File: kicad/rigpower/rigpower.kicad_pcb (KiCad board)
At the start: 2 copper layers, 66 x 54.6 mm, 11 parts, among them J1 Conn_01x02, J2 Conn_01x02, J3 Conn_01x02, J4 Conn_01x02, J5 Conn_01x02

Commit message: drawing improved
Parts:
- added REF**: SolderWirePad_single_0-8mmDrill, Wire_Pads:SolderWirePad_single_0-8mmDrill, B.Cu at (157.5, 111.1)
- added REF**: SolderWirePad_single_0-8mmDrill, Wire_Pads:SolderWirePad_single_0-8mmDrill, B.Cu at (163.2, 130.8)
- added REF**: SolderWirePad_single_0-8mmDrill, Wire_Pads:SolderWirePad_single_0-8mmDrill, B.Cu at (152.4, 130.8)
- added REF**: SolderWirePad_single_0-8mmDrill, Wire_Pads:SolderWirePad_single_0-8mmDrill, B.Cu at (144.1, 111.1)
- added REF**: SolderWirePad_single_0-8mmDrill, Wire_Pads:SolderWirePad_single_0-8mmDrill, B.Cu at (174.6, 111.1)
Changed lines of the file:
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@@
-(kicad_pcb (version 20171130) (host pcbnew 5.0.1)
+(kicad_pcb (version 20171130) (host pcbnew 5.1.0)
   (general
     (thickness 1.6)
-    (drawings 40)
+    (drawings 49)
     (tracks 10)
     (zones 0)
-    (modules 11)
+    (modules 16)
     (nets 11)
   )
@@
     (zone_45_only no)
     (trace_min 0.2)
-    (segment_width 0.2)
-    (edge_width 0.15)
     (via_size 0.8)
     (via_drill 0.4)
@@
     (uvia_min_size 0.2)
     (uvia_min_drill 0.1)
+    (edge_width 0.15)
+    (segment_width 0.2)
     (pcb_text_width 0.3)
     (pcb_text_size 1.5 1.5)
@@
     (mod_text_size 1 1)
     (mod_text_width 0.15)
-    (pad_size 1.7 1.7)
-    (pad_drill 1)
+    (pad_size 1.99898 1.99898)
+    (pad_drill 0)
     (pad_to_mask_clearance 0.051)
     (solder_mask_min_width 0.25)
@@
     (add_net "Net-(J5-Pad2)")
   )
+  (module Wire_Pads:SolderWirePad_single_0-8mmDrill (layer B.Cu)
+    (at 157.48 111.125)
+    (fp_text reference REF** (at 0 2.54) (layer B.SilkS) hide
+      (effects (font (size 1 1) (thickness 0.15)) (justify mirror))
+    )
+    (fp_text value SolderWirePad_single_0-8mmDrill (at 0 -2.54) (layer B.Fab)
+      (effects (font (size 1 1) (thickness 0.15)) (justify mirror))
+    )
+    (pad 1 smd circle (at 0 0) (size 1.99898 1.99898) (layers B.Cu B.Paste B.Mask))
+  )
+  (module Wire_Pads:SolderWirePad_single_0-8mmDrill (layer B.Cu)
+    (at 163.195 130.81)
+    (fp_text reference REF** (at 0 2.54) (layer B.SilkS) hide
+      (effects (font (size 1 1) (thickness 0.15)) (justify mirror))
+    )
+    (fp_text value SolderWirePad_single_0-8mmDrill (at 0 -2.54) (layer B.Fab)
+      (effects (font (size 1 1) (thickness 0.15)) (justify mirror))
+    )
+    (pad 1 smd circle (at 0 0) (size 1.99898 1.99898) (layers B.Cu B.Paste B.Mask))
+  )
+  (module Wire_Pads:SolderWirePad_single_0-8mmDrill (layer B.Cu)
+    (at 152.4 130.81)
+    (fp_text reference REF** (at 0 2.54) (layer B.SilkS) hide
+      (effects (font (size 1 1) (thickness 0.15)) (justify mirror))
+    )
+    (fp_text value SolderWirePad_single_0-8mmDrill (at 0 -2.54) (layer B.Fab)
+      (effects (font (size 1 1) (thickness 0.15)) (justify mirror))
+    )
+    (pad 1 smd circle (at 0 0) (size 1.99898 1.99898) (layers B.Cu B.Paste B.Mask))
+  )
+  (module Wire_Pads:SolderWirePad_single_0-8mmDrill (layer B.Cu)
+    (at 144.145 111.125)
+    (fp_text reference REF** (at 0 2.54) (layer B.SilkS) hide
+      (effects (font (size 1 1) (thickness 0.15)) (justify mirror))
+    )
+    (fp_text value SolderWirePad_single_0-8mmDrill (at 0 -2.54) (layer B.Fab)
+      (effects (font (size 1 1) (thickness 0.15)) (justify mirror))
+    )
+    (pad 1 smd circle (at 0 0) (size 1.99898 1.99898) (layers B.Cu B.Paste B.Mask))
+  )
+  (module Wire_Pads:SolderWirePad_single_0-8mmDrill (layer B.Cu)
+    (at 174.625 111.125)
+    (fp_text reference REF** (at 0 2.54) (layer B.SilkS) hide
+      (effects (font (size 1 1) (thickness 0.15)) (justify mirror))
+    )
+    (fp_text value SolderWirePad_single_0-8mmDrill (at 0 -2.54) (layer B.Fab)
+      (effects (font (size 1 1) (thickness 0.15)) (justify mirror))
+    )
+    (pad 1 smd circle (at 0 0) (size 1.99898 1.99898) (layers B.Cu B.Paste B.Mask))
+  )
   (module MountingHole:MountingHole_5mm (layer F.Cu)
     (at 144.78 96.52)
@@
     (pad 1 np_thru_hole circle (at 0 0) (size 5 5) (drill 5) (layers *.Cu *.Mask))
   )
+  (gr_line (start 157.48 110.744) (end 157.48 114.046) (layer B.SilkS) (width 1))
+  (gr_line (start 174.625 110.744) (end 144.145 110.744) (layer B.SilkS) (width 1))
+  (gr_line (start 144.145 110.744) (end 138.176 116.84) (layer B.SilkS) (width 1))
+  (gr_line (start 174.625 110.744) (end 178.181 113.919) (layer B.SilkS) (width 1))
+  (gr_line (start 135.128 128.27) (end 129.032 128.27) (layer B.SilkS) (width 1))
+  (gr_line (start 135.128 118.11) (end 129.032 118.11) (layer B.SilkS) (width 1))
+  (gr_line (start 147.32 117.094) (end 147.32 123.825) (layer B.SilkS) (width 1))
+  (gr_line (start 157.48 117.348) (end 157.48 124.079) (layer B.SilkS) (width 1))
+  (gr_line (start 178.435 117.348) (end 178.435 124.079) (layer B.SilkS) (width 1))
+  (gr_line (start 168.275 117.094) (end 168.275 123.825) (layer B.SilkS) (width 1))
+  (gr_line (start 173.228 96.52) (end 167.132 96.52) (layer B.SilkS) (width 1))
+  (gr_line (start 134.874 96.52) (end 128.778 96.52) (layer B.SilkS) (width 1))
+  (gr_line (start 135.128 106.68) (end 129.032 106.68) (layer B.SilkS) (width 1))
+  (gr_line (start 167.005 106.68) (end 173.228 106.68) (layer B.SilkS) (width 1))
   (gr_text - (at 178.435 135.128) (layer F.SilkS)
     (effects (font (size 1.5 1.5) (thickness 0.3)))
@@
     (effects (font (size 1.5 1.5) (thickness 0.3)))
   )
-  (gr_line (start 174.625 120.65) (end 178.435 115.57) (layer B.SilkS) (width 1))
-  (gr_line (start 161.925 120.65) (end 174.625 120.65) (layer B.SilkS) (width 1))
   (gr_text "REGULATOR OUT" (at 131.445 135.89) (layer F.SilkS)
     (effects (font (size 1.5 1.5) (thickness 0.3)))
@@
   (gr_line (start 152.4 130.81) (end 163.195 130.81) (layer B.SilkS) (width 1))
   (gr_line (start 148.59 127) (end 152.4 130.81) (layer B.SilkS) (width 1))
-  (gr_line (start 138.43 127) (end 146.05 127) (layer B.SilkS) (width 1))
-  (gr_line (start 158.75 116.84) (end 161.925 120.65) (layer B.SilkS) (width 1))
-  (gr_line (start 153.67 119.38) (end 156.845 116.84) (layer B.SilkS) (width 1))
-  (gr_line (start 139.065 119.38) (end 153.67 119.38) (layer B.SilkS) (width 1))
+  (gr_line (start 138.684 128.016) (end 145.923 126.365) (layer B.SilkS) (width 1))
   (gr_line (start 160.02 96.52) (end 162.56 96.52) (layer B.SilkS) (width 1))
   (gr_line (start 162.56 106.68) (end 139.7 106.68) (layer B.SilkS) (width 1))

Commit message: rigpower renewal
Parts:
- removed the REF** at (157.5, 111.1)
- removed the REF** at (157.5, 96.5)
- removed the REF** at (163.2, 130.8)
- removed the REF** at (152.4, 130.8)
- removed the REF** at (144.1, 111.1)
- removed the REF** at (174.6, 111.1)
- removed the REF** at (144.8, 96.5)
- added J6: Conn_01x02, TerminalBlock:TerminalBlock_bornier-2_P5.08mm, F.Cu at (153.7, 101.6)
- added REF**: MountingHole_2.5mm, MountingHole:MountingHole_2.5mm, F.Cu at (119.4, 42.5)
- added REF**: MountingHole_2.5mm, MountingHole:MountingHole_2.5mm, F.Cu at (149.2, 42.5)
- J4, J5: footprint lib:TerminalBlock_P10.16mm -> lib:TerminalBlock_P9.5mm
- moved J1 33.0 mm to (149.2, 86.4)
- moved REF** 30.2 mm to (158.8, 67.9)
- moved J4 29.1 mm to (118.7, 120.0)
- moved J5 28.5 mm to (140.3, 120.0)
- moved REF** 25.6 mm to (158.8, 125.7)
- moved REF** 22.2 mm to (110.5, 67.9)
- moved J2 21.7 mm to (119.4, 76.2)
- moved J3 21.1 mm to (119.4, 98.4)
- moved REF** 15.3 mm to (110.5, 125.7)
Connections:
- J4 pad 1: Net-(J4-Pad1) -> (no net)
- J4 pad 2: Net-(J4-Pad2) -> (no net)
- J5 pad 1: Net-(J5-Pad1) -> (no net)
- J5 pad 2: Net-(J5-Pad2) -> (no net)
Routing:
- net Net-(J2-Pad1): track 10.2 -> 51.4 mm
- net Net-(J2-Pad2): track 10.2 -> 44.2 mm
- net Net-(J5-Pad2): track 10.2 -> 0.00 mm
- net Net-(J5-Pad1): track 10.2 -> 0.00 mm
- net Net-(J4-Pad2): track 10.2 -> 0.00 mm
- net Net-(J4-Pad1): track 10.2 -> 0.00 mm
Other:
- board size 66 x 54.6 mm -> 53.3 x 88.3 mm
- board text added: "+ REGULATOR OUT -"
- board text added: "- AUX +"
- board text added: "- POWER SOURCE +"
- board text added: "- REGULATOR IN +"
- board text added: "M/B + -"
- board text added: "PCIe + -"
- board text removed: "+"
- board text removed: "-"
- board text removed: "MOTHERBOARD"
- board text removed: "PCI EXPRESS"
- board text removed: "POWER SOURCE"
- board text removed: "REGULATOR IN"
- board text removed: "REGULATOR OUT"

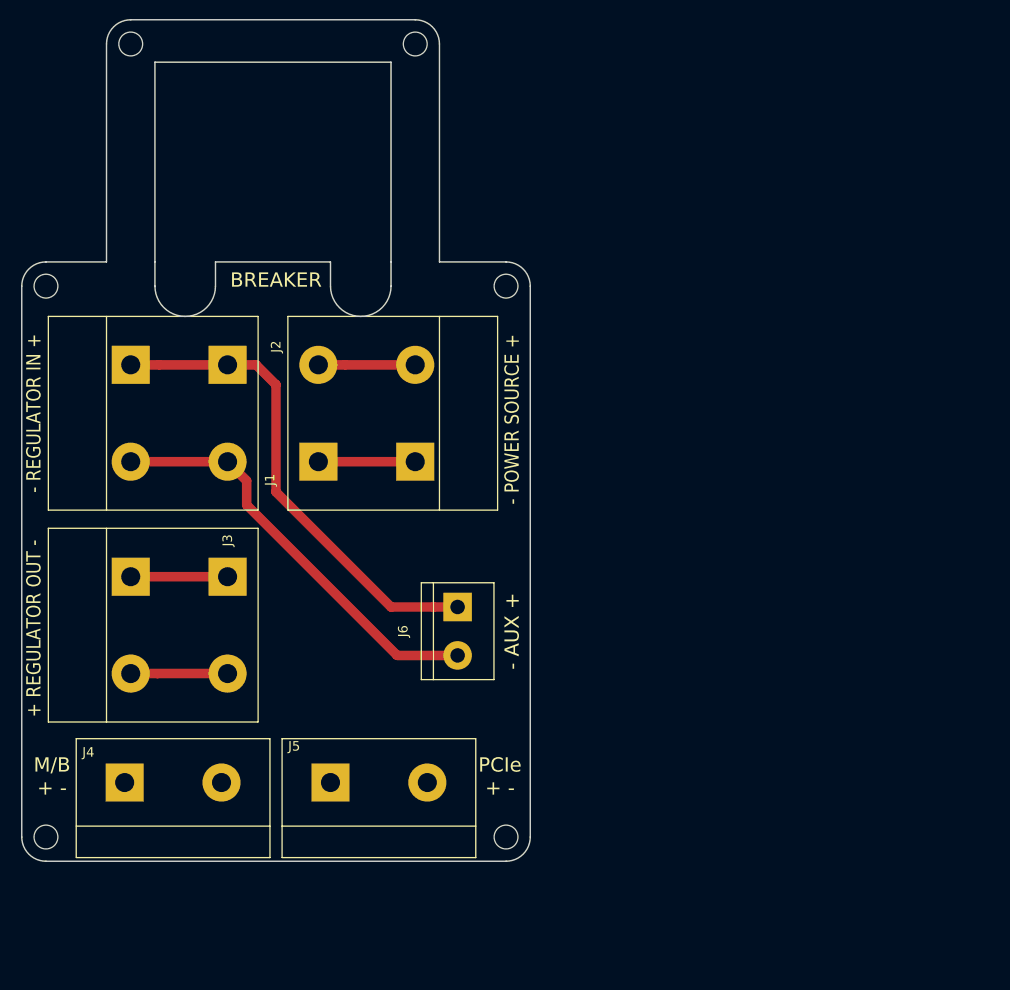
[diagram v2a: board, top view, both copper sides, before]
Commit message: change for 2p circuit breaker
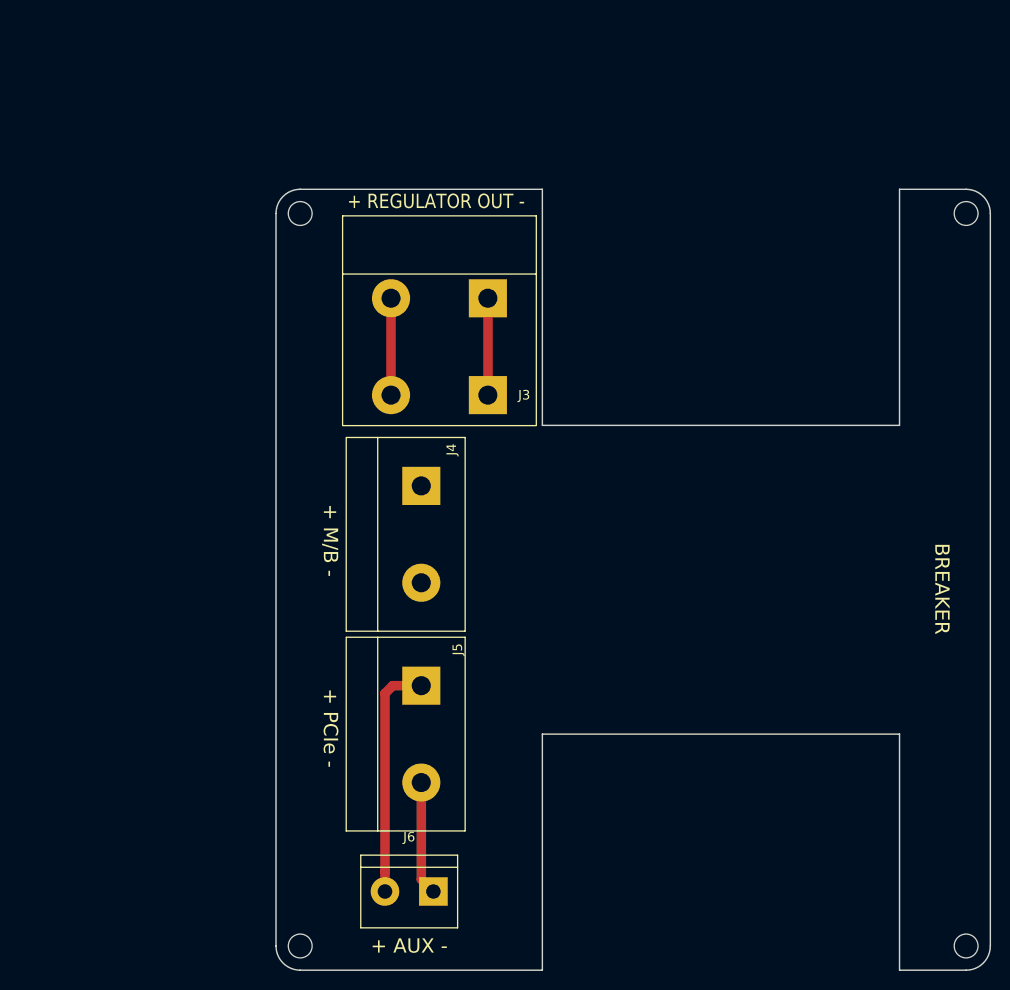
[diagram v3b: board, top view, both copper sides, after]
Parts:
- removed J1, J2: Conn_01x02, lib:TerminalBlock_P10.16mm
- removed the REF** at (110.5, 67.9)
- removed the REF** at (158.8, 67.9)
- moved REF** 110.9 mm to (207.0, 137.2), turned to 270 degrees
- moved REF** 89.4 mm to (207.0, 60.3), turned to 270 degrees
- moved REF** 70.6 mm to (137.2, 60.3), turned to 270 degrees
- moved J3 47.5 mm to (156.8, 69.2), turned to 180 degrees
- moved J4 44.0 mm to (149.9, 88.9), turned to 270 degrees
- moved J6 30.0 mm to (151.1, 131.4), turned to 180 degrees
- moved REF** 24.4 mm to (137.2, 137.2), turned to 270 degrees
- moved J5 13.9 mm to (149.9, 109.9), turned to 270 degrees
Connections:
- J5 pad 1: (no net) -> Net-(J5-Pad1)
- J5 pad 2: (no net) -> Net-(J5-Pad2)
- J6 pad 1: Net-(J2-Pad1) -> Net-(J5-Pad2)
- J6 pad 2: Net-(J2-Pad2) -> Net-(J5-Pad1)
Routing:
- net Net-(J2-Pad1): track 51.4 -> 0.00 mm
- net Net-(J2-Pad2): track 44.2 -> 0.00 mm
- net Net-(J5-Pad1): track 0.00 -> 24.9 mm
- net Net-(J5-Pad2): track 0.00 -> 12.0 mm
- net Net-(J1-Pad2): track 10.2 -> 0.00 mm
- net Net-(J1-Pad1): track 10.2 -> 0.00 mm
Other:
- board size 53.3 x 88.3 mm -> 74.9 x 81.9 mm
- board text added: "+ AUX -"
- board text added: "+ M/B -"
- board text added: "+ PCIe -"
- board text removed: "- AUX +"
- board text removed: "- POWER SOURCE +"
- board text removed: "- REGULATOR IN +"
- board text removed: "M/B + -"
- board text removed: "PCIe + -"
